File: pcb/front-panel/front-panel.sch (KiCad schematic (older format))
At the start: 4 parts, among them J1 HEADER-1x05, U1 ER-OLED1602-4W, U2 TSL2561

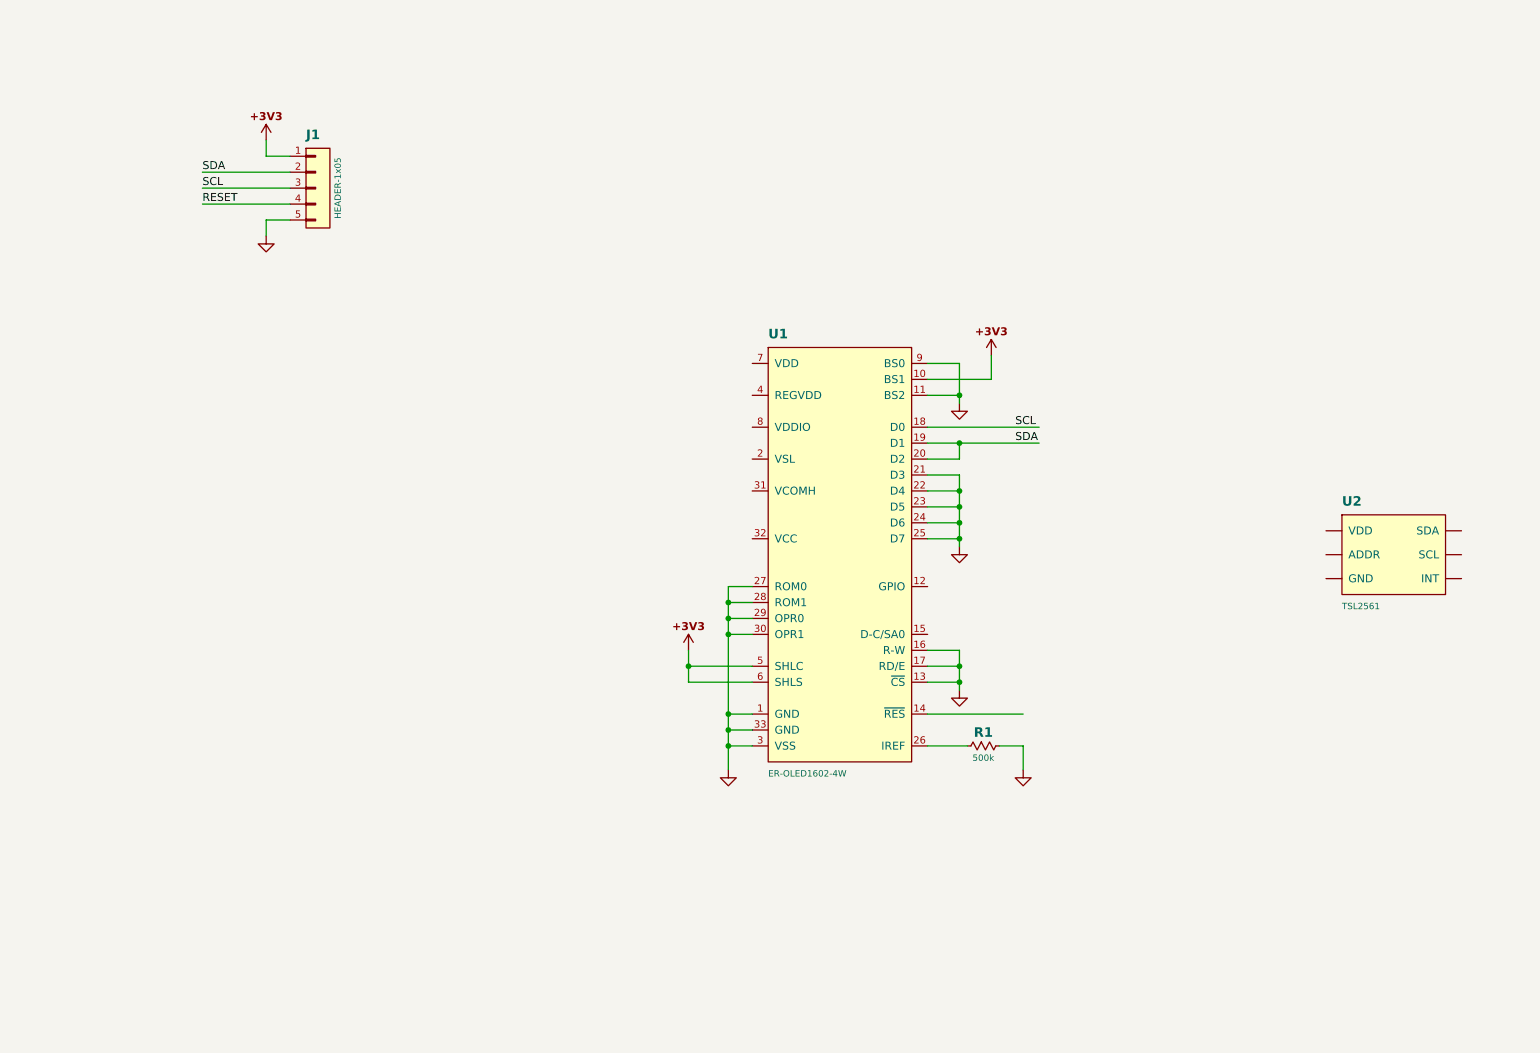
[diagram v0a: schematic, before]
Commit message: Added schematic for front panel pcb
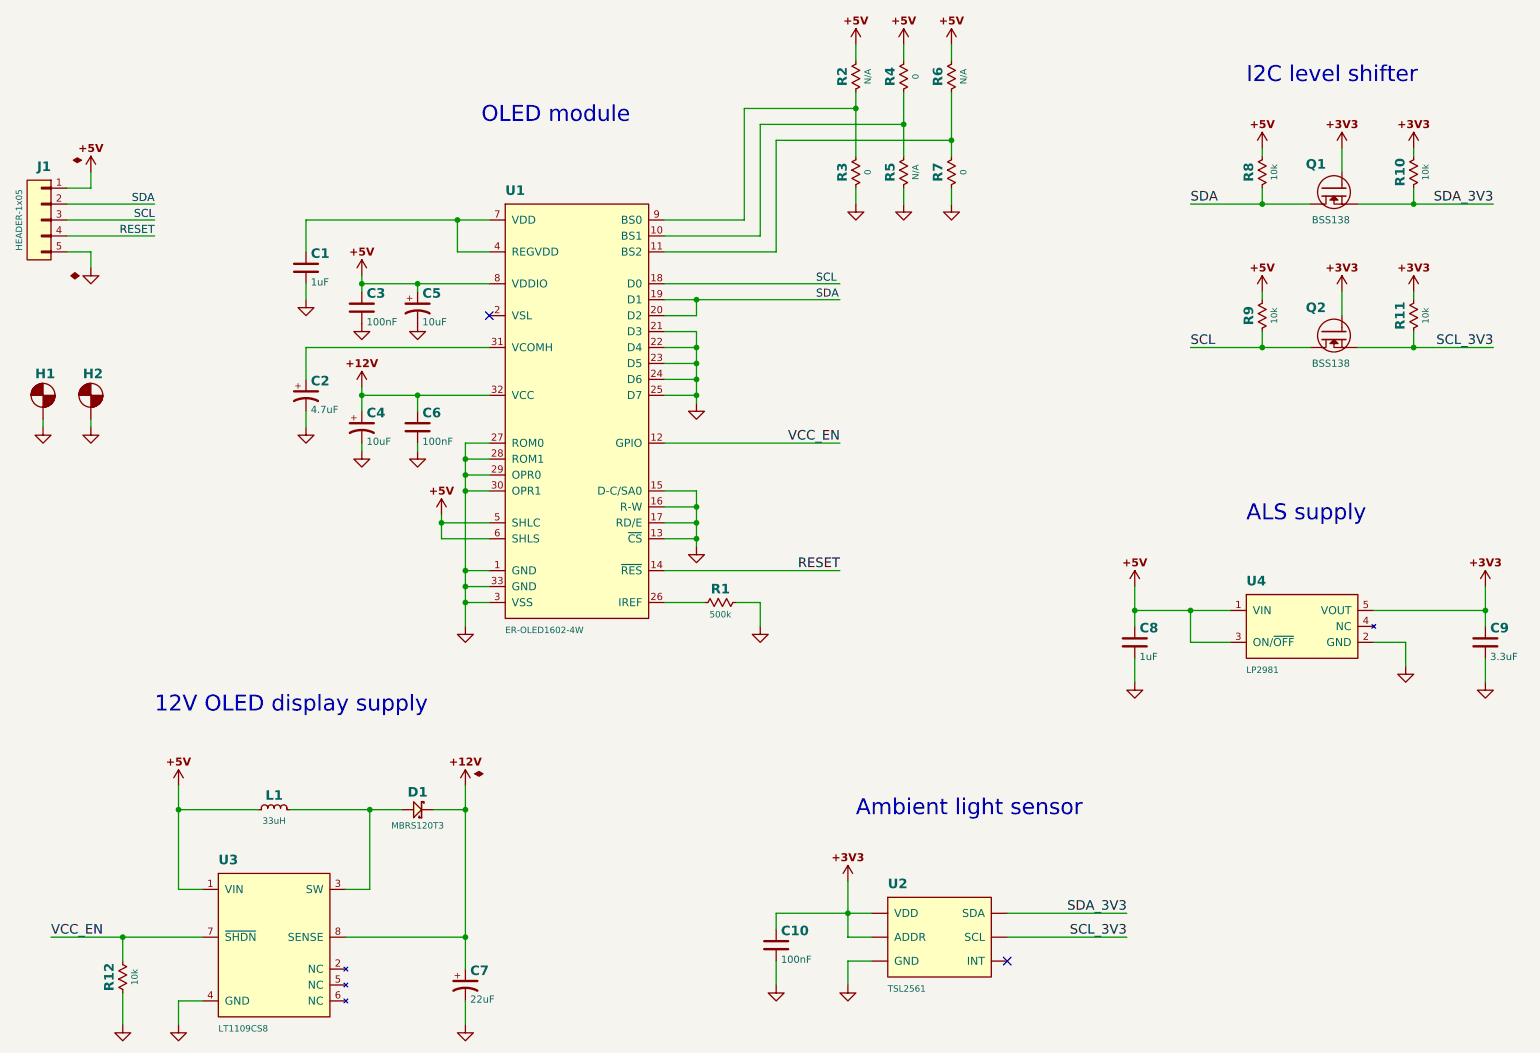
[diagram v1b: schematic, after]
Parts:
- added C1, C8: 1uF, SMT:C-0805, symbol CAP
- added C10, C3, C6: 100nF, SMT:C-0603, symbol CAP
- added C2: 4.7uF, SMT:CPL-1206, symbol CAP-E
- added C4, C5: 10uF, SMT:CPL-0805, symbol CAP-E
- added C7: 22uF, symbol CAP-E
- added C9: 3.3uF, SMT:C-0805, symbol CAP
- added D1: MBRS120T3, symbol SCHOTTKY
- added H1, H2: Hole, Conn-Wire-Pads:Hole-Screw-#2, symbol Hole
- added L1: 33uH, symbol INDUCTOR
- added Q1, Q2: BSS138, SMT-SOT:SOT23, symbol N-MOSFET
- added R10, R11, R12, R8, R9: 10k, SMT:R-0603, symbol RESISTOR
- added R2, R5, R6: N/A, SMT:R-0603, symbol RESISTOR
- added R3, R4, R7: 0, SMT:R-0603, symbol RESISTOR
- added U3: LT1109CS8, SMT-SOIC:SOIC8, symbol LT1109CS8
- added U4: LP2981, SMT-SOT:SOT23-5, symbol LP2981
- R1: footprint (none) -> SMT:R-0603
- U2: footprint SMT-DFN:6 -> SMT-DFN:DFN6
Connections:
- net labels added: +12V, +5V, SCL_3V3, SDA_3V3, SUP_+12V, SUP_+5V, SUP_GND, VCC_EN
- wire segments 41 -> 124
- no-connect marks 0 -> 2
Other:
- note added: "12V OLED display supply"
- note added: "ALS supply"
- note added: "Ambient light sensor"
- note added: "I2C level shifter"
- note added: "OLED module"
- moved on the sheet: J1, R1, U1, U2

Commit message: Changed sheet size to US letter
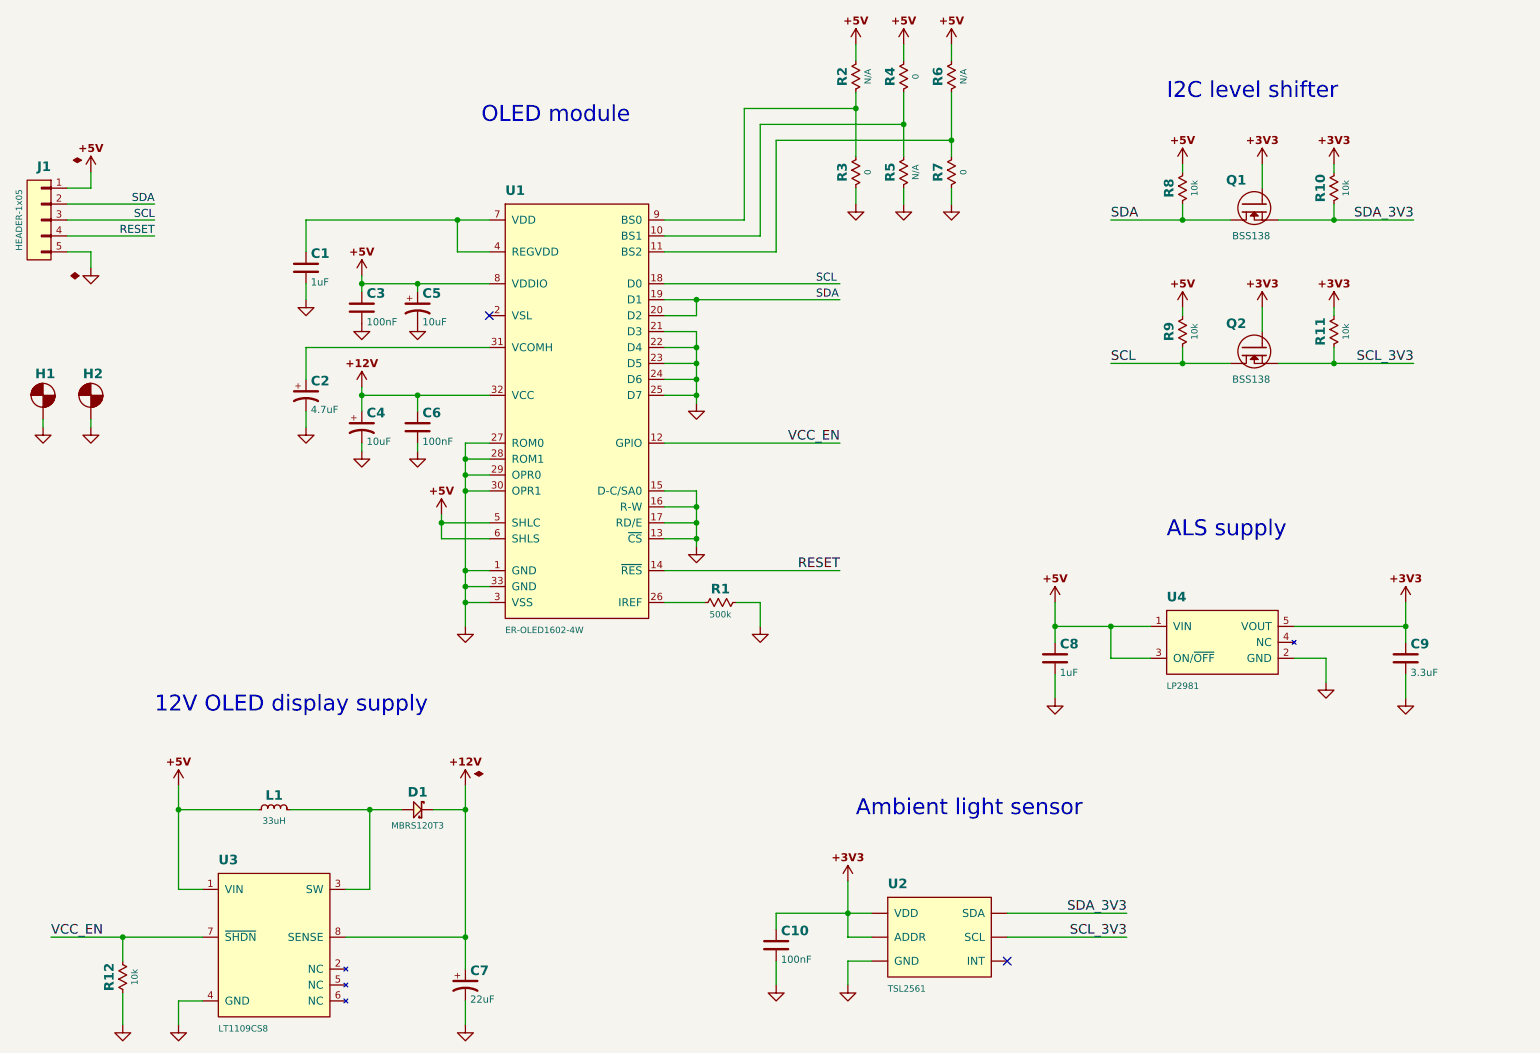
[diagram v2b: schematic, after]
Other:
- moved on the sheet: C8, C9, Q1, Q2, R10, R11, R8, R9, U4

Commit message: Added front panel pcb
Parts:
- removed C10: 100nF, SMT:C-0603, symbol CAP
- removed C8: 1uF, SMT:C-0805, symbol CAP
- removed C9: 3.3uF, SMT:C-0805, symbol CAP
- removed H1, H2: Hole, Conn-Wire-Pads:Hole-Screw-#2, symbol Hole
- removed Q1, Q2: BSS138, SMT-SOT:SOT23, symbol N-MOSFET
- removed R10, R11, R8, R9: 10k, SMT:R-0603, symbol RESISTOR
- removed U2: TSL2561, SMT-DFN:DFN6, symbol TSL2561
- removed U3: LT1109CS8, SMT-SOIC:SOIC8, symbol LT1109CS8
- removed U4: LP2981, SMT-SOT:SOT23-5, symbol LP2981
- added J2, J3, J4: HEADER-1x01, Conn-Wire-Pads:SolderPad-100x500, symbol HEADER-1x01
- added J5: HEADER-1x01, Conn-Wire-Pads:SolderPad-100x150, symbol HEADER-1x01
- added TP1: 12V, Conn-Wire-Pads:TEST-POINT-50, symbol TEST-POINT
- added TP2: GND, Conn-Wire-Pads:TEST-POINT-50, symbol TEST-POINT
- added U2: LT1109CS8-12, SMT-SOIC:SOIC8, symbol LT1109CS8
- C7: footprint (none) -> SMT:CPL-2312
- D1: footprint (none) -> SMT:DO-214-AA; PART - -> MBRS120T3
- J1: Family Connector -> Virtual
- L1: footprint (none) -> SMT:IND-CD54; PART - -> CR54NP-330LC
- R2, R5, R6: value N/A -> DNP
- U1: Part (none) -> ER-OLED1602-4W
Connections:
- net +12V: now also TP1.1 (P1), U2.8 (SENSE)
- net +5V: now also U2.1 (VIN)
- net GND: now also TP2.1 (P1), U2.4 (GND)
- net VCC_EN: now also U2.7 (~SHDN)
- net SW_12V: now reaches D1.A, L1.2
- net SW_12V: now also U2.3 (SW)
- no-connect marks 2 -> 5
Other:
- note removed: "ALS supply"
- note removed: "Ambient light sensor"
- note removed: "I2C level shifter"
- moved on the sheet: C1, C2, C3, C4, C5, C6, C7, D1, J1, L1, R1, R12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
